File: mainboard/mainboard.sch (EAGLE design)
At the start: 49 parts, among them T2 NPN_BC817,215, X1 JST-XH-06-PIN-LONG-PAD

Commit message: farnell attrs
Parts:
- EMIT: FARNELL - -> 1212763
- RECEIVE: FARNELL - -> 3152856
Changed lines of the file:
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@@
 </part>
 <part name="EMIT" library="rhoban" deviceset="CONNEC_1X02" device="JST-ZH">
-<attribute name="FARNELL" value="-"/>
+<attribute name="FARNELL" value="1212763"/>
 </part>
 <part name="RECEIVE" library="rhoban" deviceset="CONNEC_1X02" device="JST-ZH">
-<attribute name="FARNELL" value="-"/>
+<attribute name="FARNELL" value="3152856"/>
 </part>
 <part name="T2" library="rhoban" deviceset="NPN" device="_BC817,215">

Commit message: Farnel ATTRs
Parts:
- U$1, U$10, U$11, U$5: FARNELL (none) -> 2673327RL
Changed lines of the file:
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@@
 <part name="U$8" library="rhoban" deviceset="CPOL_EU" device="PANASONIC_D8"/>
 <part name="U$9" library="rhoban" deviceset="CPOL_EU" device="PANASONIC_D8"/>
-<part name="U$1" library="rhoban" deviceset="DRV5023FAEDBZRQ1" device=""/>
+<part name="U$1" library="rhoban" deviceset="DRV5023FAEDBZRQ1" device="">
+<attribute name="FARNELL" value="2673327RL"/>
+</part>
 <part name="R1" library="rhoban" deviceset="RESISTANCE" device="-R0805" value="10K">
 <attribute name="FARNELL" value="2447553"/>
 </part>
-<part name="U$5" library="rhoban" deviceset="DRV5023FAEDBZRQ1" device=""/>
+<part name="U$5" library="rhoban" deviceset="DRV5023FAEDBZRQ1" device="">
+<attribute name="FARNELL" value="2673327RL"/>
+</part>
 <part name="R2" library="rhoban" deviceset="RESISTANCE" device="-R0805" value="10K">
 <attribute name="FARNELL" value="2447553"/>
 </part>
-<part name="U$10" library="rhoban" deviceset="DRV5023FAEDBZRQ1" device=""/>
+<part name="U$10" library="rhoban" deviceset="DRV5023FAEDBZRQ1" device="">
+<attribute name="FARNELL" value="2673327RL"/>
+</part>
 <part name="R3" library="rhoban" deviceset="RESISTANCE" device="-R0805" value="10K">
 <attribute name="FARNELL" value="2447553"/>
 </part>
-<part name="U$11" library="rhoban" deviceset="DRV5023FAEDBZRQ1" device=""/>
+<part name="U$11" library="rhoban" deviceset="DRV5023FAEDBZRQ1" device="">
+<attribute name="FARNELL" value="2673327RL"/>
+</part>
 <part name="R7" library="rhoban" deviceset="RESISTANCE" device="-R0805" value="10K">
 <attribute name="FARNELL" value="2447553"/>
@@
 </plain>
 <instances>
-<instance part="U$1" gate="G$1" x="0" y="0"/>
+<instance part="U$1" gate="G$1" x="0" y="0">
+<attribute name="FARNELL" x="0" y="0" size="1.778" layer="96" display="off"/>
+</instance>
 <instance part="R1" gate="G$1" x="20.32" y="5.08" rot="R90">
 <attribute name="FARNELL" x="20.32" y="5.08" size="1.778" layer="96" rot="R90" display="off"/>
 </instance>
-<instance part="U$5" gate="G$1" x="0" y="-22.86"/>
+<instance part="U$5" gate="G$1" x="0" y="-22.86">
+<attribute name="FARNELL" x="0" y="-22.86" size="1.778" layer="96" display="off"/>
+</instance>
 <instance part="R2" gate="G$1" x="20.32" y="-17.78" rot="R90">
 <attribute name="FARNELL" x="20.32" y="-17.78" size="1.778" layer="96" rot="R90" display="off"/>
 </instance>
-<instance part="U$10" gate="G$1" x="73.66" y="0"/>
+<instance part="U$10" gate="G$1" x="73.66" y="0">
+<attribute name="FARNELL" x="73.66" y="0" size="1.778" layer="96" display="off"/>
+</instance>
 <instance part="R3" gate="G$1" x="93.98" y="5.08" rot="R90">
 <attribute name="FARNELL" x="93.98" y="5.08" size="1.778" layer="96" rot="R90" display="off"/>
 </instance>
-<instance part="U$11" gate="G$1" x="73.66" y="-22.86"/>
+<instance part="U$11" gate="G$1" x="73.66" y="-22.86">
+<attribute name="FARNELL" x="73.66" y="-22.86" size="1.778" layer="96" display="off"/>
+</instance>
 <instance part="R7" gate="G$1" x="93.98" y="-17.78" rot="R90">
 <attribute name="FARNELL" x="93.98" y="-17.78" size="1.778" layer="96" rot="R90" display="off"/>

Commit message: Updating BOMs and ATTRs
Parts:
- U$7, U$8, U$9: value (none) -> 220uF; FARNELL (none) -> 1850103
- X1: FARNELL (none) -> -
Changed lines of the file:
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@@
 <attribute name="FARNELL" value="2496946"/>
 </part>
-<part name="U$7" library="rhoban" deviceset="CPOL_EU" device="PANASONIC_D8"/>
-<part name="X1" library="Rembrandt Electronics - JST XH Connectors v1-0" deviceset="JST-XH-06-PIN" device="-LONG-PAD"/>
-<part name="U$8" library="rhoban" deviceset="CPOL_EU" device="PANASONIC_D8"/>
-<part name="U$9" library="rhoban" deviceset="CPOL_EU" device="PANASONIC_D8"/>
+<part name="U$7" library="rhoban" deviceset="CPOL_EU" device="PANASONIC_D8" value="220uF">
+<attribute name="FARNELL" value="1850103"/>
+</part>
+<part name="X1" library="Rembrandt Electronics - JST XH Connectors v1-0" deviceset="JST-XH-06-PIN" device="-LONG-PAD">
+<attribute name="FARNELL" value="-"/>
+</part>
+<part name="U$8" library="rhoban" deviceset="CPOL_EU" device="PANASONIC_D8" value="220uF">
+<attribute name="FARNELL" value="1850103"/>
+</part>
+<part name="U$9" library="rhoban" deviceset="CPOL_EU" device="PANASONIC_D8" value="220uF">
+<attribute name="FARNELL" value="1850103"/>
+</part>
 <part name="U$1" library="rhoban" deviceset="DRV5023FAEDBZRQ1" device="">
 <attribute name="FARNELL" value="2673327RL"/>
@@
 <attribute name="FARNELL" x="2.54" y="-30.48" size="1.778" layer="96" display="off"/>
 </instance>
-<instance part="U$7" gate="G$1" x="40.64" y="25.4"/>
-<instance part="U$8" gate="G$1" x="43.18" y="-2.54"/>
-<instance part="U$9" gate="G$1" x="43.18" y="-33.02"/>
+<instance part="U$7" gate="G$1" x="40.64" y="25.4">
+<attribute name="FARNELL" x="40.64" y="25.4" size="1.778" layer="96" display="off"/>
+</instance>
+<instance part="U$8" gate="G$1" x="43.18" y="-2.54">
+<attribute name="FARNELL" x="43.18" y="-2.54" size="1.778" layer="96" display="off"/>
+</instance>
+<instance part="U$9" gate="G$1" x="43.18" y="-33.02">
+<attribute name="FARNELL" x="43.18" y="-33.02" size="1.778" layer="96" display="off"/>
+</instance>
 </instances>
 <busses>
@@
 <instance part="X1" gate="-3" x="7.62" y="2.54"/>
 <instance part="X1" gate="-4" x="7.62" y="0"/>
-<instance part="X1" gate="-5" x="7.62" y="-2.54"/>
+<instance part="X1" gate="-5" x="7.62" y="-2.54">
+<attribute name="FARNELL" x="7.62" y="-2.54" size="1.778" layer="96" display="off"/>
+</instance>
 <instance part="X1" gate="-6" x="7.62" y="-5.08"/>
 </instances>

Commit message: Adding multiplexer on mainboard, sampling charge current, separate com ces
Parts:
- added C4: 1000pF, SparkFun-Passives:CAP0805
- added R20: 2K, SparkFun-Resistors:RESISTOR0805
- added R21: 3K, SparkFun-Resistors:RESISTOR0805
- added SENSE: ACS712, rhoban:ACS712
- added U1: CD4051BM, rhoban:CD4051BM
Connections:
- new net ADDR1: MAPLE.14, U1.A
- new net ADDR2: U1.B
- new net ADDR3: MAPLE.2, U1.C
- new net ADDR4: MAPLE.31
- new net CHARGE_CUR: R20.2, R21.1, U1.6
- new net COM_CE1: COM1.CE
- new net COM_CE2: COM2.CE, MAPLE.3
- new net COM_CE3: COM3.CE, MAPLE.9
- new net MUX: MAPLE.8, U1.COM_OUT/IN
- new net N$24: R20.1, SENSE.VIOUT
- new net N$26: U1.7
- new net N$27: C4.1, SENSE.FILTER
- new net VIN_KICKER: SENSE.IN+, X1-2.S
- net 3.3: now also U1.VDD
- net BAT: now also U1.5; no longer MAPLE.9
- net CAP: now also U1.4; no longer MAPLE.3
- net COM_CE: no longer COM1.CE, COM2.CE, COM3.CE
- net GND: now also C4.2, R21.2, SENSE.GND, U1.INH, U1.VEE, U1.VSS
- net HALL1: now also U1.0; no longer MAPLE.14
- net HALL2: now also U1.1; no longer MAPLE.8
- net HALL3: now also U1.2; no longer MAPLE.2
- net HALL4: now also U1.3; no longer MAPLE.31
- net VCC: now also SENSE.VCC
- net VIN: now also SENSE.IN-; no longer X1-2.S

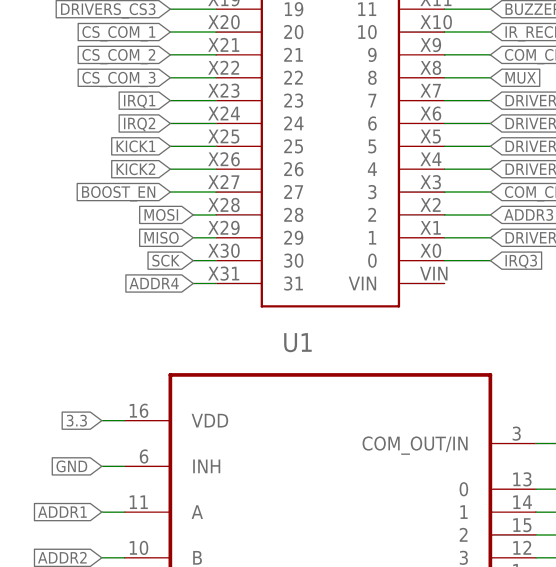
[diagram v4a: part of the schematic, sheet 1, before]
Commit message: Fixing mux addr, drivers #
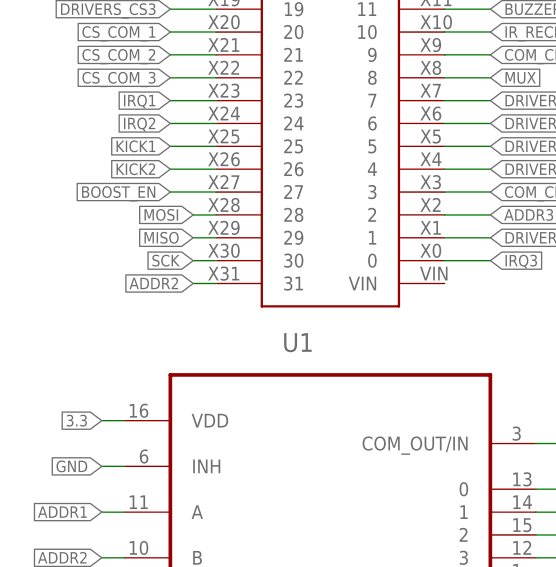
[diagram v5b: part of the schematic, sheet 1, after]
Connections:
- removed net ADDR4: MAPLE.31
- net ADDR2: now also MAPLE.31
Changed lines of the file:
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@@
 <label x="-66.04" y="45.72" size="1.27" layer="95" rot="R180" xref="yes"/>
+</segment>
+<segment>
+<pinref part="MAPLE" gate="G$1" pin="31"/>
+<wire x1="-53.34" y1="76.2" x2="-55.88" y2="76.2" width="0.1524" layer="91"/>
+<label x="-55.88" y="76.2" size="1.27" layer="95" rot="R180" xref="yes"/>
 </segment>
 </net>
@@
 </segment>
 </net>
-<net name="ADDR4" class="0">
-<segment>
-<pinref part="MAPLE" gate="G$1" pin="31"/>
-<wire x1="-53.34" y1="76.2" x2="-55.88" y2="76.2" width="0.1524" layer="91"/>
-<label x="-55.88" y="76.2" size="1.27" layer="95" rot="R180" xref="yes"/>
-</segment>
-</net>

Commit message: Using mos driver on kicker board
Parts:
- removed X1: JST-XH-06-PIN-LONG-PAD, Rembrandt Electronics - JST XH Connectors v1-0:JST-XH-06-PIN-LONG-PAD
- added X2: JST-XH-07-PIN-LONG-PAD, Rembrandt Electronics - JST XH Connectors v1-0:JST-XH-07-PIN-LONG-PAD
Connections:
- net 12V: now also X2-3.S
- net BOOST_EN: now also X2-4.S; no longer X1-3.S
- net CAP: now also X2-7.S; no longer X1-6.S
- net GND: now also X2-1.S; no longer X1-1.S
- net KICK1: now also X2-5.S; no longer X1-4.S
- net KICK2: now also X2-6.S; no longer X1-5.S
- net VIN_KICKER: now also X2-2.S; no longer X1-2.S
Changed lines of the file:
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@@
 <attribute name="FARNELL" value="1850103"/>
-</part>
-<part name="X1" library="Rembrandt Electronics - JST XH Connectors v1-0" deviceset="JST-XH-06-PIN" device="-LONG-PAD">
-<attribute name="FARNELL" value="-"/>
 </part>
 <part name="U$8" library="rhoban" deviceset="CPOL_EU" device="PANASONIC_D8" value="220uF">
@@
 <attribute name="VALUE" value=" "/>
 </part>
+<part name="X2" library="Rembrandt Electronics - JST XH Connectors v1-0" deviceset="JST-XH-07-PIN" device="-LONG-PAD"/>
 </parts>
 <sheets>
@@
 </plain>
 <instances>
-<instance part="X1" gate="-1" x="7.62" y="7.62"/>
-<instance part="X1" gate="-2" x="7.62" y="5.08"/>
-<instance part="X1" gate="-3" x="7.62" y="2.54"/>
-<instance part="X1" gate="-4" x="7.62" y="0"/>
-<instance part="X1" gate="-5" x="7.62" y="-2.54">
-<attribute name="FARNELL" x="7.62" y="-2.54" size="1.778" layer="96" display="off"/>
-</instance>
-<instance part="X1" gate="-6" x="7.62" y="-5.08"/>
 <instance part="SENSE" gate="G$1" x="-7.62" y="-27.94">
 <attribute name="FARNELL" x="-7.62" y="-27.94" size="1.778" layer="96" display="off"/>
@@
 <attribute name="FARNELL" x="40.64" y="-17.78" size="1.778" layer="96" display="off"/>
 </instance>
+<instance part="X2" gate="-1" x="0" y="7.62"/>
+<instance part="X2" gate="-2" x="0" y="5.08"/>
+<instance part="X2" gate="-3" x="0" y="2.54"/>
+<instance part="X2" gate="-4" x="0" y="0"/>
+<instance part="X2" gate="-5" x="0" y="-2.54"/>
+<instance part="X2" gate="-6" x="0" y="-5.08"/>
+<instance part="X2" gate="-7" x="0" y="-7.62"/>
 </instances>
 <busses>
@@
 <net name="KICK2" class="0">
 <segment>
-<pinref part="X1" gate="-5" pin="S"/>
-<wire x1="5.08" y1="-2.54" x2="0" y2="-2.54" width="0.1524" layer="91"/>
-<label x="0" y="-2.54" size="1.27" layer="95" rot="R180" xref="yes"/>
+<pinref part="X2" gate="-6" pin="S"/>
+<wire x1="-2.54" y1="-5.08" x2="-5.08" y2="-5.08" width="0.1524" layer="91"/>
+<label x="-5.08" y="-5.08" size="1.27" layer="95" rot="R180" xref="yes"/>
 </segment>
 </net>
 <net name="GND" class="2">
-<segment>
-<pinref part="X1" gate="-1" pin="S"/>
-<wire x1="5.08" y1="7.62" x2="0" y2="7.62" width="0.1524" layer="91"/>
-<label x="0" y="7.62" size="1.27" layer="95" rot="R180" xref="yes"/>
-</segment>
 <segment>
 <pinref part="SENSE" gate="G$1" pin="GND"/>
@@
 <label x="50.8" y="-17.78" size="1.27" layer="95" xref="yes"/>
 </segment>
+<segment>
+<pinref part="X2" gate="-1" pin="S"/>
+<wire x1="-2.54" y1="7.62" x2="-5.08" y2="7.62" width="0.1524" layer="91"/>
+<label x="-5.08" y="7.62" size="1.27" layer="95" rot="R180" xref="yes"/>
+</segment>
 </net>
 <net name="VIN" class="2">
@@
 <net name="KICK1" class="0">
 <segment>
-<pinref part="X1" gate="-4" pin="S"/>
-<wire x1="5.08" y1="0" x2="0" y2="0" width="0.1524" layer="91"/>
-<label x="0" y="0" size="1.27" layer="95" rot="R180" xref="yes"/>
+<pinref part="X2" gate="-5" pin="S"/>
+<wire x1="-2.54" y1="-2.54" x2="-5.08" y2="-2.54" width="0.1524" layer="91"/>
+<label x="-5.08" y="-2.54" size="1.27" layer="95" rot="R180" xref="yes"/>
 </segment>
 </net>
 <net name="CAP" class="0">
 <segment>
-<pinref part="X1" gate="-6" pin="S"/>
-<wire x1="5.08" y1="-5.08" x2="0" y2="-5.08" width="0.1524" layer="91"/>
-<label x="0" y="-5.08" size="1.27" layer="95" rot="R180" xref="yes"/>
+<pinref part="X2" gate="-7" pin="S"/>
+<wire x1="-2.54" y1="-7.62" x2="-5.08" y2="-7.62" width="0.1524" layer="91"/>
+<label x="-5.08" y="-7.62" size="1.27" layer="95" rot="R180" xref="yes"/>
 </segment>
 </net>
 <net name="BOOST_EN" class="0">
 <segment>
-<pinref part="X1" gate="-3" pin="S"/>
-<wire x1="5.08" y1="2.54" x2="0" y2="2.54" width="0.1524" layer="91"/>
-<label x="0" y="2.54" size="1.27" layer="95" rot="R180" xref="yes"/>
+<pinref part="X2" gate="-4" pin="S"/>
+<wire x1="-2.54" y1="0" x2="-5.08" y2="0" width="0.1524" layer="91"/>
+<label x="-5.08" y="0" size="1.27" layer="95" rot="R180" xref="yes"/>
 </segment>
 </net>
@@
 </segment>
 <segment>
-<pinref part="X1" gate="-2" pin="S"/>
-<wire x1="5.08" y1="5.08" x2="0" y2="5.08" width="0.1524" layer="91"/>
-<label x="0" y="5.08" size="1.27" layer="95" rot="R180" xref="yes"/>
-</segment>
-</net>
+<pinref part="X2" gate="-2" pin="S"/>
+<wire x1="-2.54" y1="5.08" x2="-5.08" y2="5.08" width="0.1524" layer="91"/>
+<label x="-5.08" y="5.08" size="1.27" layer="95" rot="R180" xref="yes"/>
+</segment>
+</net>
+<net name="12V" class="0">
+<segment>
+<pinref part="X2" gate="-3" pin="S"/>
+<wire x1="-2.54" y1="2.54" x2="-5.08" y2="2.54" width="0.1524" layer="91"/>
+<label x="-5.08" y="2.54" size="1.27" layer="95" rot="R180" xref="yes"/>
+</segment>
+</net>
